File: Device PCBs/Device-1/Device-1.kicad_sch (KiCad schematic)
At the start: 52 parts, among them J1 Conn_01x04_Female, J2 Conn_01x04_Female, U1 EBYTE_E32-433T20D, U10 signle_via, U11 signle_via, U12 signle_via, U13 signle_via, U14 signle_via, U15 signle_via, U16 signle_via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

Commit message: PCBway gerbers are finished.
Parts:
- added R16, R17, R18: 3.3k, Resistor_SMD:R_1206_3216Metric, symbol Device:R
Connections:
- net EBYTE_RX: now also R16.2; no longer ArduinoNano1.7 (D4), D6.2 (A)
- net M0: now also R18.2; no longer ArduinoNano1.9 (D6), D9.2 (A)
- net M1: now also R17.2; no longer ArduinoNano1.8 (D5), D8.2 (A)
- new net: ArduinoNano1.8 (D5), D8.2 (A), R17.1
- new net: ArduinoNano1.7 (D4), D6.2 (A), R16.1
- new net: ArduinoNano1.9 (D6), D9.2 (A), R18.1
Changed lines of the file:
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@@
   (junction (at 213.995 61.595) (diameter 0) (color 0 0 0 0)
   )
+  (junction (at 222.885 66.675) (diameter 0) (color 0 0 0 0)
+  )
   (junction (at 213.995 34.925) (diameter 0) (color 0 0 0 0)
   )
   (junction (at 110.871 146.177) (diameter 0) (color 0 0 0 0)
   )
+  (junction (at 227.33 69.215) (diameter 0) (color 0 0 0 0)
+  )
+  (junction (at 218.44 64.135) (diameter 0) (color 0 0 0 0)
+  )
   (junction (at 222.885 34.925) (diameter 0) (color 0 0 0 0)
   )
@@
   (junction (at 209.55 59.055) (diameter 0) (color 0 0 0 0)
   )
-  (junction (at 227.33 69.215) (diameter 0) (color 0 0 0 0)
-  )
   (junction (at 59.182 73.406) (diameter 0) (color 0 0 0 0)
   )
@@
   )
   (junction (at 76.327 91.821) (diameter 0) (color 0 0 0 0)
-  )
-  (junction (at 222.885 66.675) (diameter 0) (color 0 0 0 0)
-  )
-  (junction (at 218.44 64.135) (diameter 0) (color 0 0 0 0)
   )
   (junction (at 61.087 70.866) (diameter 0) (color 0 0 0 0)
@@
     (stroke (width 0) (type default) (color 0 0 0 0))
   )
+  (wire (pts (xy 194.945 66.675) (xy 196.85 66.675))
+    (stroke (width 0) (type default) (color 0 0 0 0))
+  )
   (wire (pts (xy 224.155 87.63) (xy 224.155 79.375))
     (stroke (width 0) (type default) (color 0 0 0 0))
@@
     (stroke (width 0) (type default) (color 0 0 0 0))
   )
+  (wire (pts (xy 204.47 69.215) (xy 227.33 69.215))
+    (stroke (width 0) (type default) (color 0 0 0 0))
+  )
   (wire (pts (xy 126.111 146.177) (xy 126.111 150.622))
     (stroke (width 0) (type default) (color 0 0 0 0))
@@
     (stroke (width 1.5) (type default) (color 0 0 0 0))
   )
+  (wire (pts (xy 194.945 64.135) (xy 196.85 64.135))
+    (stroke (width 0) (type default) (color 0 0 0 0))
+  )
+  (wire (pts (xy 204.47 64.135) (xy 218.44 64.135))
+    (stroke (width 0) (type default) (color 0 0 0 0))
+  )
   (wire (pts (xy 227.33 53.34) (xy 227.33 69.215))
     (stroke (width 0) (type default) (color 0 0 0 0))
@@
     (stroke (width 0) (type default) (color 0 0 0 0))
   )
-  (wire (pts (xy 194.945 64.135) (xy 218.44 64.135))
-    (stroke (width 0) (type default) (color 0 0 0 0))
-  )
   (wire (pts (xy 59.182 80.391) (xy 59.182 73.406))
     (stroke (width 0) (type default) (color 0 0 0 0))
@@
   )
   (wire (pts (xy 110.871 146.177) (xy 110.871 153.162))
-    (stroke (width 0) (type default) (color 0 0 0 0))
-  )
-  (wire (pts (xy 194.945 66.675) (xy 222.885 66.675))
     (stroke (width 0) (type default) (color 0 0 0 0))
   )
@@
     (stroke (width 1.5) (type solid) (color 0 0 0 0))
   )
+  (wire (pts (xy 204.47 66.675) (xy 222.885 66.675))
+    (stroke (width 0) (type default) (color 0 0 0 0))
+  )
   (wire (pts (xy 254.635 74.295) (xy 257.175 74.295))
     (stroke (width 0) (type default) (color 0 0 0 0))
@@
     (stroke (width 0) (type default) (color 0 0 0 0))
   )
-  (wire (pts (xy 194.945 69.215) (xy 227.33 69.215))
-    (stroke (width 0) (type default) (color 0 0 0 0))
-  )
   (polyline (pts (xy 80.518 19.05) (xy 80.518 45.72))
     (stroke (width 0.67) (type default) (color 0 0 0 0))
@@
   )
   (wire (pts (xy 219.075 71.755) (xy 229.235 71.755))
+    (stroke (width 0) (type default) (color 0 0 0 0))
+  )
+  (wire (pts (xy 194.945 69.215) (xy 196.85 69.215))
     (stroke (width 0) (type default) (color 0 0 0 0))
   )
@@
     )
     (pin "1")
+  )
+  (symbol (lib_id "Device:R") (at 200.66 66.675 270) (unit 1)
+    (in_bom yes) (on_board yes)
+    (property "Reference" "R17" (id 0) (at 205.105 65.405 90)
+      (effects (font (size 1.27 1.27)) (justify left))
+    )
+    (property "Value" "3.3k" (id 1) (at 198.12 66.675 90)
+      (effects (font (size 1.27 1.27)) (justify left))
+    )
+    (property "Footprint" "Resistor_SMD:R_1206_3216Metric" (id 2) (at 200.66 64.897 90)
+      (effects (font (size 1.27 1.27)) hide)
+    )
+    (property "Datasheet" "~" (id 3) (at 200.66 66.675 0)
+      (effects (font (size 1.27 1.27)) hide)
+    )
+    (pin "1")
+    (pin "2")
   )
   (symbol (lib_id "Device:R") (at 213.995 40.64 180) (unit 1)
@@
     (pin "2")
   )
+  (symbol (lib_id "Device:R") (at 200.66 69.215 270) (unit 1)
+    (in_bom yes) (on_board yes)
+    (property "Reference" "R18" (id 0) (at 205.105 67.945 90)
+      (effects (font (size 1.27 1.27)) (justify left))
+    )
+    (property "Value" "3.3k" (id 1) (at 198.12 69.215 90)
+      (effects (font (size 1.27 1.27)) (justify left))
+    )
+    (property "Footprint" "Resistor_SMD:R_1206_3216Metric" (id 2) (at 200.66 67.437 90)
+      (effects (font (size 1.27 1.27)) hide)
+    )
+    (property "Datasheet" "~" (id 3) (at 200.66 69.215 0)
+      (effects (font (size 1.27 1.27)) hide)
+    )
+    (pin "1")
+    (pin "2")
+  )
   (symbol (lib_id "Interface_UART:MAX487E") (at 76.327 73.406 0) (unit 1)
     (in_bom yes) (on_board yes) (fields_autoplaced)
@@
     (pin "1")
   )
+  (symbol (lib_id "Device:R") (at 200.66 64.135 270) (unit 1)
+    (in_bom yes) (on_board yes)
+    (property "Reference" "R16" (id 0) (at 205.105 62.865 90)
+      (effects (font (size 1.27 1.27)) (justify left))
+    )
+    (property "Value" "3.3k" (id 1) (at 198.12 64.135 90)
+      (effects (font (size 1.27 1.27)) (justify left))
+    )
+    (property "Footprint" "Resistor_SMD:R_1206_3216Metric" (id 2) (at 200.66 62.357 90)
+      (effects (font (size 1.27 1.27)) hide)
+    )
+    (property "Datasheet" "~" (id 3) (at 200.66 64.135 0)
+      (effects (font (size 1.27 1.27)) hide)
+    )
+    (pin "1")
+    (pin "2")
+  )
   (symbol (lib_id "Device:R") (at 210.185 90.17 0) (unit 1)
     (in_bom yes) (on_board yes)
@@
       (reference "R15") (unit 1) (value "3.3k") (footprint "Resistor_SMD:R_1206_3216Metric")
     )
+    (path "/e8ab1eab-ea16-4d2c-a674-f53ebe0de364"
+      (reference "R16") (unit 1) (value "3.3k") (footprint "Resistor_SMD:R_1206_3216Metric")
+    )
+    (path "/20038aed-8b51-4cde-8284-4a47a1e4b8a7"
+      (reference "R17") (unit 1) (value "3.3k") (footprint "Resistor_SMD:R_1206_3216Metric")
+    )
+    (path "/bc7f0aa3-e429-4eca-bf37-84d35282bffe"
+      (reference "R18") (unit 1) (value "3.3k") (footprint "Resistor_SMD:R_1206_3216Metric")
+    )
     (path "/4b2fe800-2e75-48c0-bd87-5feef54a0a17"

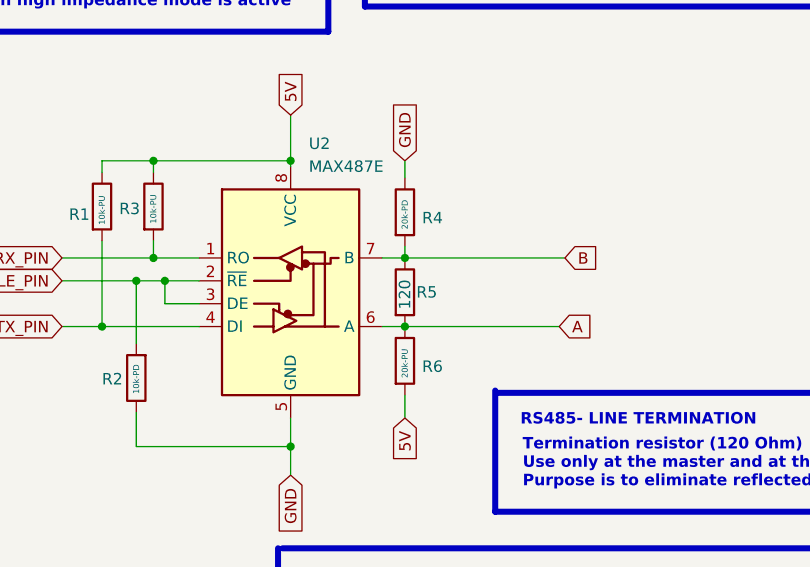
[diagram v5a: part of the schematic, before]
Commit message: Simple RS485 modbus slave is added
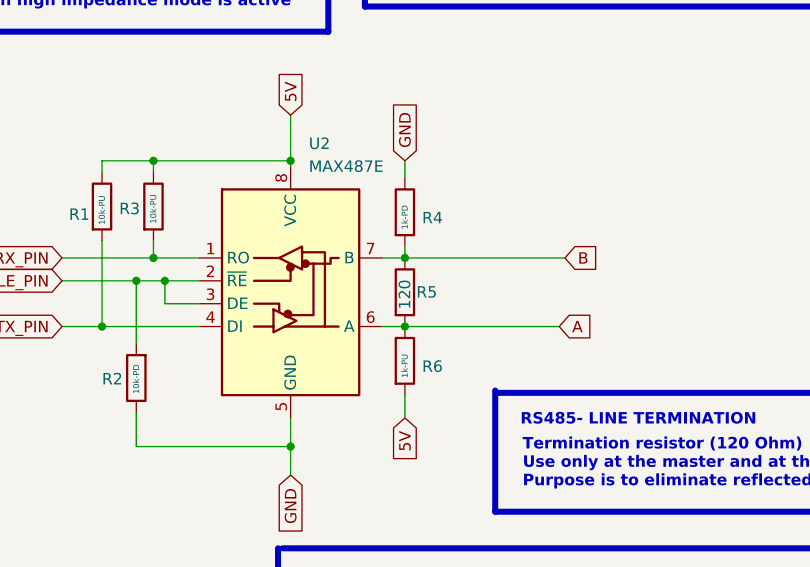
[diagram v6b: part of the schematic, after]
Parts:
- R4: value 20k-PD -> 1k-PD
- R6: value 20k-PU -> 1k-PU
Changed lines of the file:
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@@
       (effects (font (size 1.27 1.27)) (justify left))
     )
-    (property "Value" "20k-PU" (id 1) (at 89.027 84.201 90)
+    (property "Value" "1k-PU" (id 1) (at 89.027 84.201 90)
       (effects (font (size 0.67 0.67)) (justify left))
     )
@@
       (effects (font (size 1.27 1.27)) (justify left))
     )
-    (property "Value" "20k-PD" (id 1) (at 89.027 67.691 90)
+    (property "Value" "1k-PD" (id 1) (at 89.027 67.691 90)
       (effects (font (size 0.67 0.67)) (justify left))
     )
@@
     )
     (path "/c1f9c4f8-b219-4cf4-ab1c-2c5729aed676"
-      (reference "R4") (unit 1) (value "20k-PD") (footprint "Resistor_SMD:R_1206_3216Metric")
+      (reference "R4") (unit 1) (value "1k-PD") (footprint "Resistor_SMD:R_1206_3216Metric")
     )
     (path "/11bd84b1-7898-4b50-bdc5-b0c494072853"
@@
     )
     (path "/73ef84a6-fa13-46f4-a12b-a9bf8ee2afd1"
-      (reference "R6") (unit 1) (value "20k-PU") (footprint "Resistor_SMD:R_1206_3216Metric")
+      (reference "R6") (unit 1) (value "1k-PU") (footprint "Resistor_SMD:R_1206_3216Metric")
     )
     (path "/04fd6b4e-54d1-4f4d-868f-0cc46c425a4c"
